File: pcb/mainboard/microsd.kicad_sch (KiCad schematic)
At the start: 9 parts, among them U201 MIMX8MN6DVTJZAA, U702 W25Q128JVP

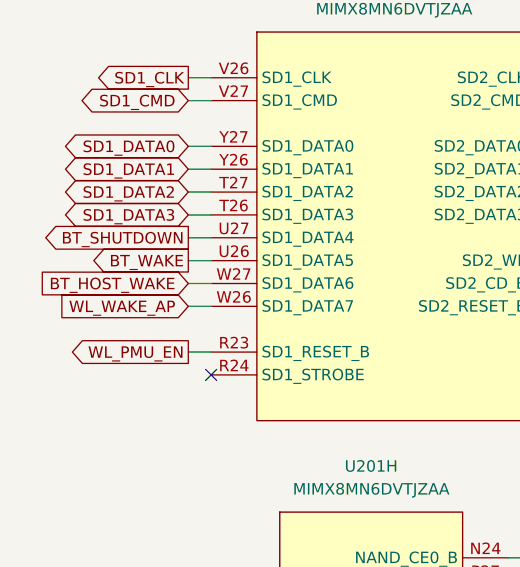
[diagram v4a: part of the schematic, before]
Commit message: Routing mainboard in progress, schematics fixes
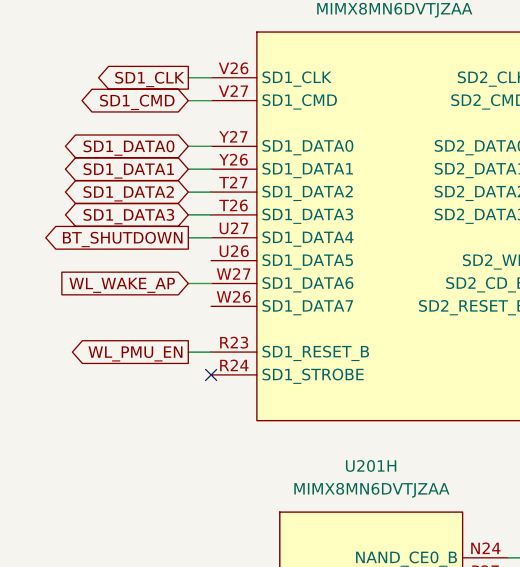
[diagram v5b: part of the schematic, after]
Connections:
- net BT_HOST_WAKE is gone; now on net WL_WAKE_AP: U201.W27 (SD1_DATA6)
- net WL_WAKE_AP: no longer U201.W26 (SD1_DATA7)
- net BT_WAKE: no longer names the net of U201.U26 (SD1_DATA5)
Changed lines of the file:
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@@
-    (stroke (width 0) (type default) (color 0 0 0 0))
-  )
-  (wire (pts (xy 73.66 78.74) (xy 76.2 78.74))
     (stroke (width 0) (type default) (color 0 0 0 0))
   )
@@
     (stroke (width 0) (type solid) (color 0 0 0 0))
   )
-  (wire (pts (xy 73.66 83.82) (xy 76.2 83.82))
+  (wire (pts (xy 73.66 81.28) (xy 76.2 81.28))
     (stroke (width 0) (type default) (color 0 0 0 0))
   )
@@
   )
   (wire (pts (xy 177.8 83.82) (xy 185.42 83.82))
-    (stroke (width 0) (type default) (color 0 0 0 0))
-  )
-  (wire (pts (xy 73.66 81.28) (xy 76.2 81.28))
     (stroke (width 0) (type default) (color 0 0 0 0))
   )
@@
     )
   )
-  (global_label "WL_WAKE_AP" (shape input) (at 73.66 83.82 180) (fields_autoplaced)
-    (effects (font (size 1.27 1.27)) (justify right))
-    (property "Intersheet References" "${INTERSHEET_REFS}" (id 0) (at 59.324 83.7406 0)
+  (global_label "WL_WAKE_AP" (shape input) (at 73.66 81.28 180) (fields_autoplaced)
+    (effects (font (size 1.27 1.27)) (justify right))
+    (property "Intersheet References" "${INTERSHEET_REFS}" (id 0) (at 59.324 81.2006 0)
       (effects (font (size 1.27 1.27)) (justify right) hide)
     )
@@
     )
   )
-  (global_label "BT_WAKE" (shape output) (at 73.66 78.74 180) (fields_autoplaced)
-    (effects (font (size 1.27 1.27)) (justify right))
-    (property "Intersheet References" "${INTERSHEET_REFS}" (id 0) (at 63.0826 78.8194 0)
-      (effects (font (size 1.27 1.27)) (justify right) hide)
-    )
-  )
   (global_label "SD_D3" (shape bidirectional) (at 119.38 73.66 0)
     (effects (font (size 1.27 1.27)) (justify left))
@@
     )
   )
-  (global_label "BT_HOST_WAKE" (shape input) (at 73.66 81.28 180) (fields_autoplaced)
-    (effects (font (size 1.27 1.27)) (justify right))
-    (property "Intersheet References" "${INTERSHEET_REFS}" (id 0) (at 57.0864 81.2006 0)
-      (effects (font (size 1.27 1.27)) (justify right) hide)
-    )
-  )
